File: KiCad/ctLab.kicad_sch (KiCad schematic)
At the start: 0 parts

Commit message: adding schematics for PM8 module
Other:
- added sheet PM8 (pm8.kicad_sch)
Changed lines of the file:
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@@
 	(paper "A3")
+	(sheet
+		(at 274.32 31.75)
+		(size 74.93 41.91)
+		(exclude_from_sim no)
+		(in_bom yes)
+		(on_board yes)
+		(dnp no)
+		(fields_autoplaced yes)
+		(stroke
+			(width 0.1524)
+			(type solid)
+		)
+		(fill
+			(color 0 0 0 0)
+		)
+		(property "Sheetname" "PM8"
+			(at 274.32 31.0384 0)
+			(show_name no)
+			(do_not_autoplace no)
+			(effects
+				(font
+					(size 1.27 1.27)
+				)
+				(justify left bottom)
+			)
+		)
+		(property "Sheetfile" "pm8.kicad_sch"
+			(at 274.32 74.2446 0)
+			(show_name no)
+			(do_not_autoplace no)
+			(effects
+				(font
+					(size 1.27 1.27)
+				)
+				(justify left top)
+			)
+		)
+		(instances
+			(project "ctLab"
+				(path "/207e0f0e-27e8-440d-b34e-edbac4dab547"
+					(page "5")
+				)
+			)
+		)
+	)
 	(sheet
 		(at 116.84 30.48)

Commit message: starting dds
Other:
- added sheet DDS (Digital Signal-Generator) (dds.kicad_sch)
- added sheet TRMSC (trsmc.kicad_sch)
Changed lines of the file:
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@@
+	)
+	(sheet
+		(at 116.84 93.98)
+		(size 54.61 38.1)
+		(exclude_from_sim no)
+		(in_bom yes)
+		(on_board yes)
+		(dnp no)
+		(fields_autoplaced yes)
+		(stroke
+			(width 0.1524)
+			(type solid)
+		)
+		(fill
+			(color 0 0 0 0)
+		)
+		(property "Sheetname" "TRMSC"
+			(at 116.84 93.2684 0)
+			(show_name no)
+			(do_not_autoplace no)
+			(effects
+				(font
+					(size 1.27 1.27)
+				)
+				(justify left bottom)
+			)
+		)
+		(property "Sheetfile" "trsmc.kicad_sch"
+			(at 116.84 132.6646 0)
+			(show_name no)
+			(do_not_autoplace no)
+			(effects
+				(font
+					(size 1.27 1.27)
+				)
+				(justify left top)
+			)
+		)
+		(instances
+			(project "ctLab"
+				(path "/207e0f0e-27e8-440d-b34e-edbac4dab547"
+					(page "7")
+				)
+			)
+		)
+	)
+	(sheet
+		(at 33.02 92.71)
+		(size 58.42 39.37)
+		(exclude_from_sim no)
+		(in_bom yes)
+		(on_board yes)
+		(dnp no)
+		(fields_autoplaced yes)
+		(stroke
+			(width 0.1524)
+			(type solid)
+		)
+		(fill
+			(color 0 0 0 0)
+		)
+		(property "Sheetname" "DDS (Digital Signal-Generator)"
+			(at 33.02 91.9984 0)
+			(show_name no)
+			(do_not_autoplace no)
+			(effects
+				(font
+					(size 1.27 1.27)
+				)
+				(justify left bottom)
+			)
+		)
+		(property "Sheetfile" "dds.kicad_sch"
+			(at 33.02 132.6646 0)
+			(show_name no)
+			(do_not_autoplace no)
+			(effects
+				(font
+					(size 1.27 1.27)
+				)
+				(justify left top)
+			)
+		)
+		(instances
+			(project "ctLab"
+				(path "/207e0f0e-27e8-440d-b34e-edbac4dab547"
+					(page "6")
+				)
+			)
+		)
 	)
 	(sheet

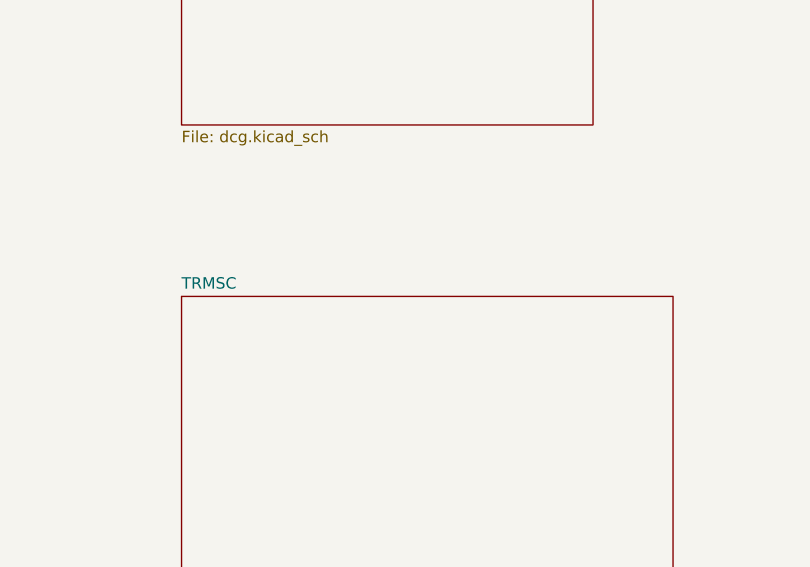
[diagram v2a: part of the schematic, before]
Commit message: cont. True-RMS Converter
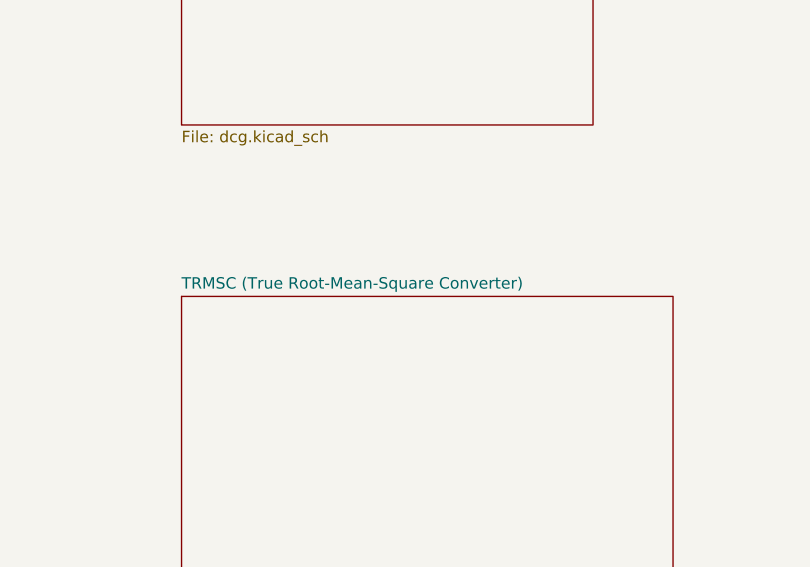
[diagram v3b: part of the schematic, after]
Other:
- sheet TRMSC renamed TRMSC (True Root-Mean-Square Converter)
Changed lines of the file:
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@@
 			(color 0 0 0 0)
 		)
-		(property "Sheetname" "TRMSC"
+		(property "Sheetname" "TRMSC (True Root-Mean-Square Converter)"
 			(at 116.84 93.2684 0)
 			(show_name no)

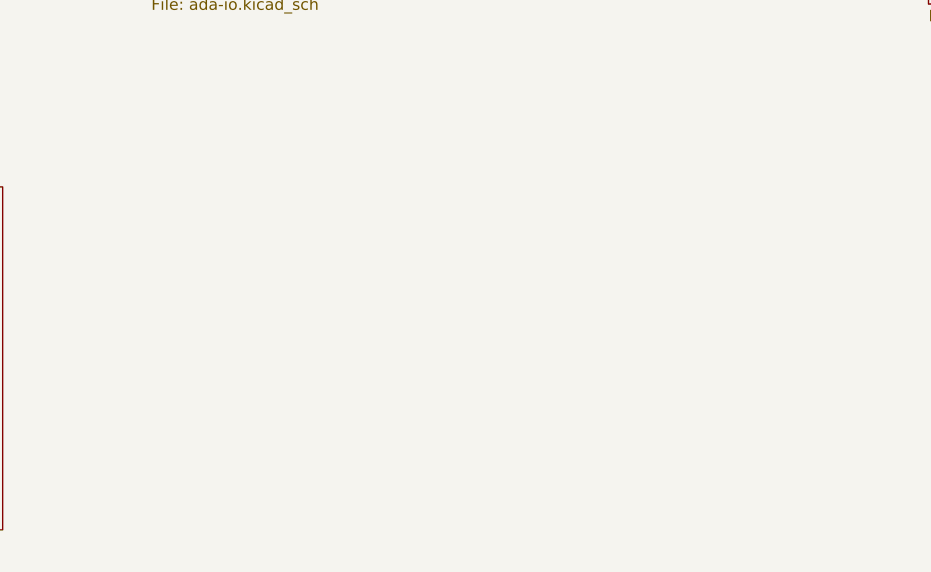
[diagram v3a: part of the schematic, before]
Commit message: starting edl schematic
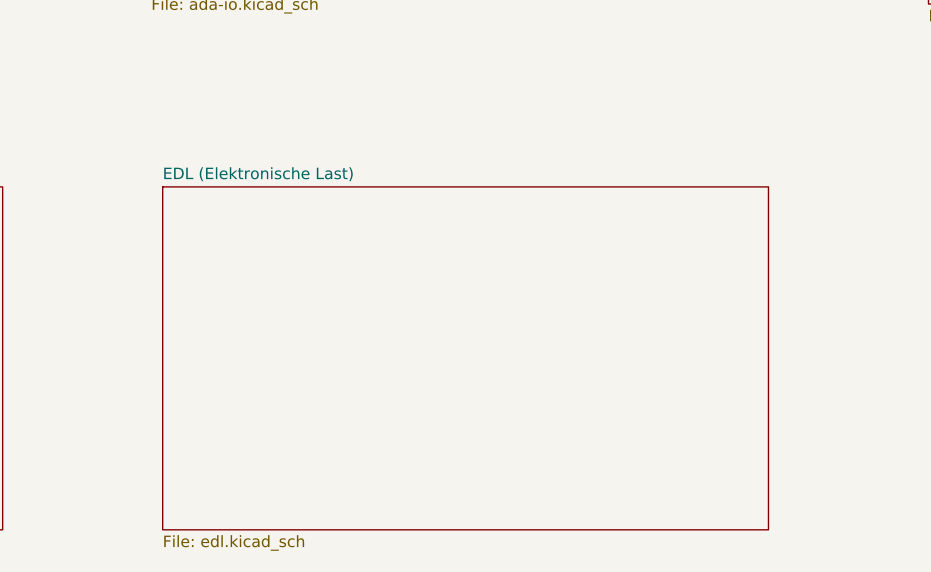
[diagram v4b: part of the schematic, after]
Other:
- added sheet EDL (Elektronische Last) (edl.kicad_sch)
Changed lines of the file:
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@@
+		)
+	)
+	(sheet
+		(at 189.23 93.98)
+		(size 67.31 38.1)
+		(exclude_from_sim no)
+		(in_bom yes)
+		(on_board yes)
+		(dnp no)
+		(fields_autoplaced yes)
+		(stroke
+			(width 0.1524)
+			(type solid)
+		)
+		(fill
+			(color 0 0 0 0)
+		)
+		(property "Sheetname" "EDL (Elektronische Last)"
+			(at 189.23 93.2684 0)
+			(show_name no)
+			(do_not_autoplace no)
+			(effects
+				(font
+					(size 1.27 1.27)
+				)
+				(justify left bottom)
+			)
+		)
+		(property "Sheetfile" "edl.kicad_sch"
+			(at 189.23 132.6646 0)
+			(show_name no)
+			(do_not_autoplace no)
+			(effects
+				(font
+					(size 1.27 1.27)
+				)
+				(justify left top)
+			)
+		)
+		(instances
+			(project "ctLab"
+				(path "/207e0f0e-27e8-440d-b34e-edbac4dab547"
+					(page "8")
+				)
+			)
 		)
 	)
